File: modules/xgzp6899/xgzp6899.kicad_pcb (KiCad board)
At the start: 2 copper layers, 24 x 20 mm, 5 parts, among them J1 SFP+, U1 XGZP6899D

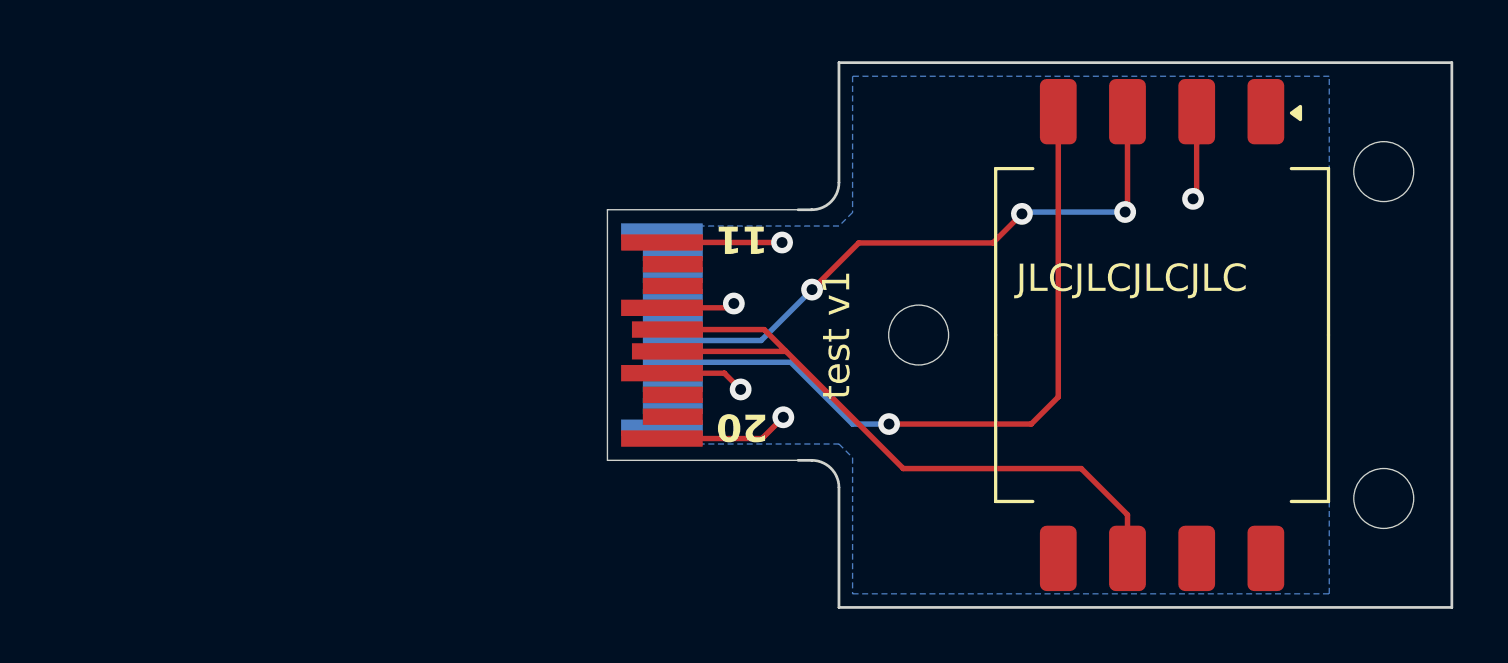
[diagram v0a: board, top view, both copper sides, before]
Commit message: Hybrid sensor module, SDP810 screw mounts (interface-v3), main board J6 adoption
Hybrid module (modules/hybrid): one L42 board that takes either an SDP810 (U1)
or an XGZP6899D (U2) on a shared site at 22 mm; fit one, never both. The SDP810
is screwed down through its body bores (M2x14, Ø2.2 NPTH) into carrier nuts at
10 and 34 mm, with B-side keepouts there. J2 is a bottom-side 1x5 pogo test pad
row, GND-SCL-3V3-SDA-GND, so a reversed jig only swaps SDA/SCL. Corners R1.

Interface v3: carrier nuts at 2.925, 10, 34 and 40 mm; the 30 mm nut is gone
(it overlaps 34 mm), which retires L32 and the xgzp6899 module. New shared
footprint sensor_module:TestPads_1x05_P2.54mm. Skeleton keepouts moved to 10/34.

Main board: J6 wired up, H7 moved to 34 mm and H9 added at 10 mm, R13 5k1
pull-up on GPIO4 (shared ~SPI_CS / UART_P2C).

Removed the breakout carrier; module CI now only scans modules/ and skips
the skeleton template.
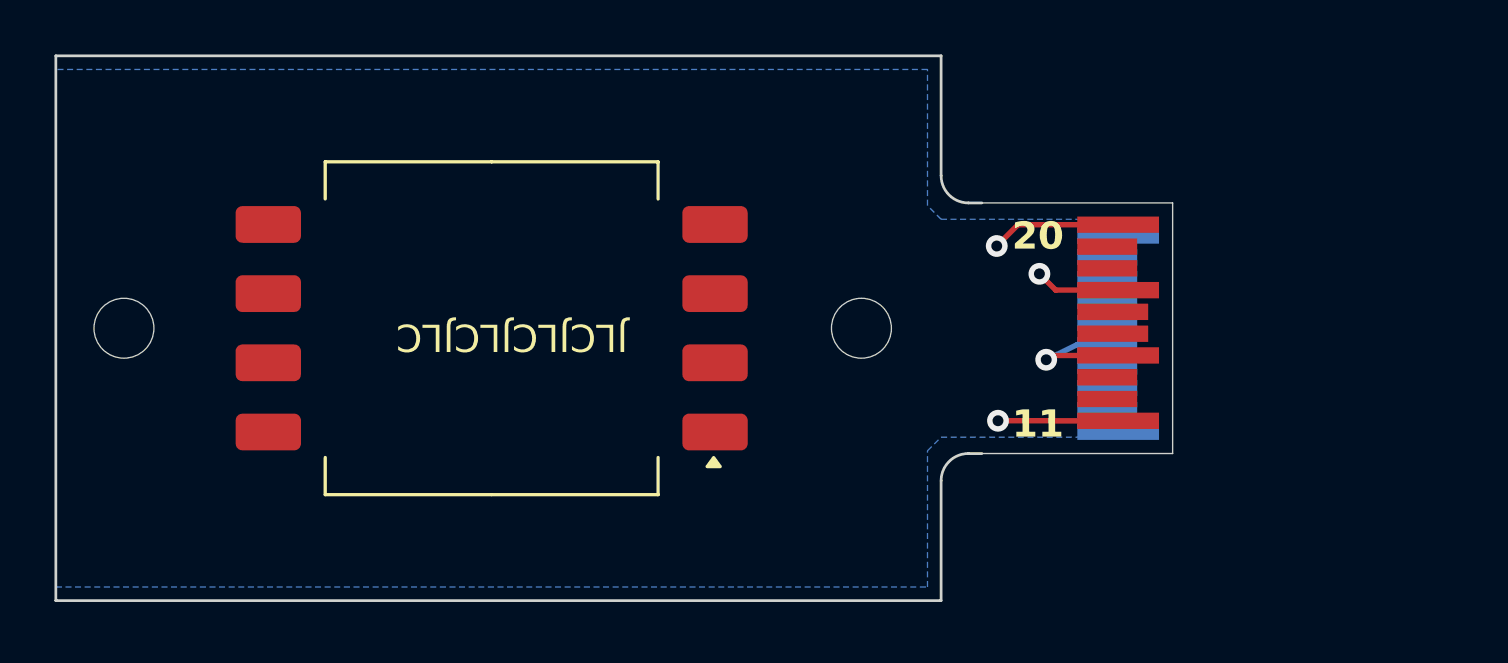
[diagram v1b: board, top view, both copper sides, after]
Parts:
- removed H3: SMSI-M2_H4mm_9774040243, MountingHole:MountingHole_2.2mm_M2
- J1: value SFP+ -> SensorModule
- moved H1 46.6 mm to (60.2, 76.0), turned to 180 degrees
- moved U1 24.6 mm to (73.8, 76.0), turned to 180 degrees
- moved J1 13.8 mm to (95.2, 76.0), turned to 0 degrees
- moved H2 2.11 mm to (87.3, 76.0), turned to 180 degrees
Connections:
- net VDD renamed +3V3
- J1 pad 6: unconnected-(J1-MOD_ABS-Pad6) -> GND
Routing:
- net SDA: track 26.0 -> 0.00 mm, vias 1 -> 0
- net +3V3: track 25.7 -> 0.00 mm
- net SCL: track 22.3 -> 0.00 mm, vias 3 -> 0
- net GND: track 18.3 -> 17.4 mm, vias 5 -> 4
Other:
- board size 24 x 20 mm -> 34 x 20 mm
- board text removed: "test v1"
